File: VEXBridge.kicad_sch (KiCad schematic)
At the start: 87 parts, among them J1 VEX V5, J10 Port 1, J11 Port 2, J12 Port 3, J13 Port 4, J14 USB_C_Receptacle_USB2.0_14P, J2 Port A, J3 Port B, J4 Port C, J5 Port D, J6 Port E, J7 Port F, J8 Port G, J9 Port H, Q1 BSS138, Q2 BSS138, Q3 BSS138, Q4 BSS138, Q5 BSS138, Q6 BSS138, Q7 BSS138, Q8 BSS138, SW1 Reset, SW2 Boot, U1 LMR33630ADDA, U2 AMS1117-3.3, U3 D3V3XA4B10LP, U4 PCA9548ADB, U6 ESP32-S3-MINI-1U, U7 MAX485E

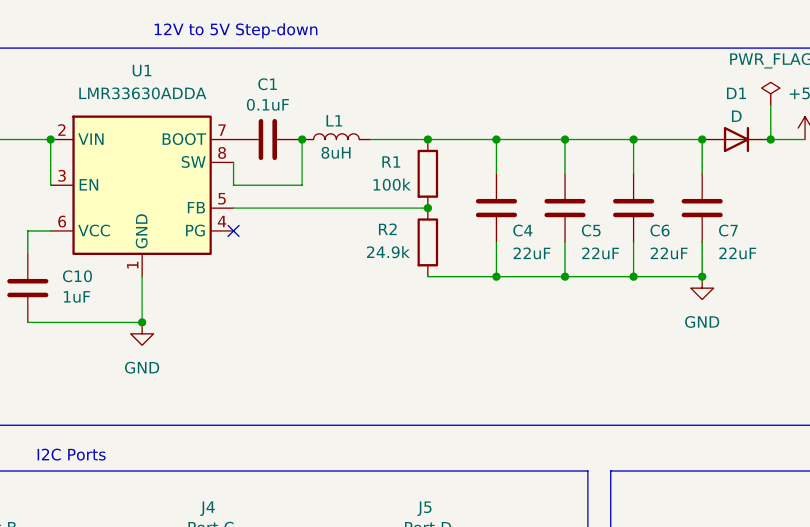
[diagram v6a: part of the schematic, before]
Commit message: Initial PCB Design w/o power rails
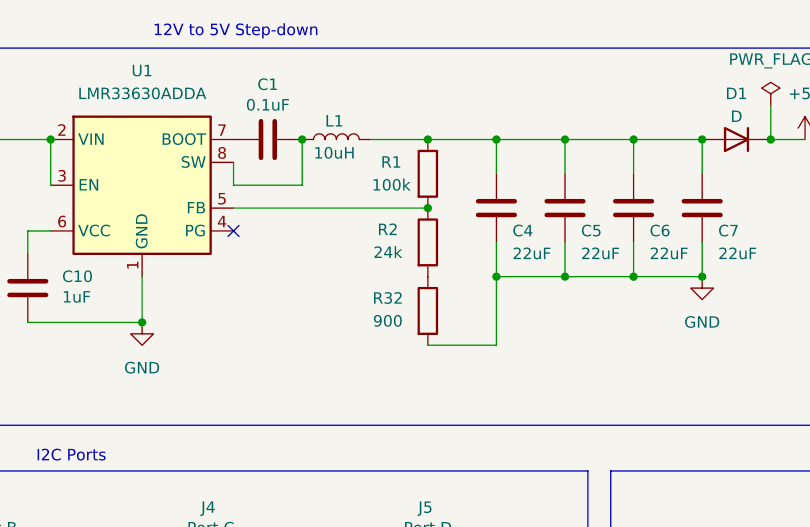
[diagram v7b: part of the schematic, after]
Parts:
- added R32: 900, Resistor_SMD:R_0805_2012Metric, symbol Device:R
- C1, C10, C2: footprint Capacitor_SMD:C_1210_3225Metric -> Capacitor_SMD:C_0603_1608Metric
- C11, C12, C13, C14, C15, C8: footprint Capacitor_SMD:C_0201_0603Metric -> Capacitor_SMD:C_0603_1608Metric
- C3: footprint Capacitor_SMD:C_1210_3225Metric -> Capacitor_SMD:C_0402_1005Metric
- C4, C5, C6, C7, C9: footprint Capacitor_SMD:C_1206_3216Metric -> Capacitor_SMD:C_0603_1608Metric
- D3, D4: footprint (none) -> LED_SMD:LED_0603_1608Metric
- JP2: footprint (none) -> Jumper:SolderJumper-3_P1.3mm_Bridged12_RoundedPad1.0x1.5mm
- L1: value 8uH -> 10uH
- Q1, Q2, Q3, Q4, Q5, Q6, Q7, Q8: footprint Package_TO_SOT_SMD:SOT-23 -> Package_TO_SOT_SMD:SOT-23-3
- R2: value 24.9k -> 24k
- SW1, SW2: footprint (none) -> Button_Switch_SMD:SW_SPST_TS-1088-xR020
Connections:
- net GND: now also R32.2; no longer R2.2
- new net: R2.2, R32.1
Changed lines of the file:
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@@
 	)
 	(junction
-		(at 182.88 43.18)
-		(diameter 0)
-		(color 0 0 0 0)
-	)
-	(junction
 		(at 24.13 167.64)
 		(diameter 0)
@@
 	)
 	(junction
+		(at 182.88 43.18)
+		(diameter 0)
+		(color 0 0 0 0)
+	)
+	(junction
 		(at 93.98 199.39)
 		(diameter 0)
@@
 	(wire
 		(pts
+			(xy 175.26 50.8) (xy 182.88 50.8)
+		)
+		(stroke
+			(width 0)
+			(type default)
+		)
+	)
+	(wire
+		(pts
 			(xy 182.88 170.18) (xy 184.15 170.18)
 		)
@@
 	(wire
 		(pts
-			(xy 175.26 43.18) (xy 182.88 43.18)
-		)
-		(stroke
-			(width 0)
-			(type default)
-		)
-	)
-	(wire
-		(pts
 			(xy 240.03 95.25) (xy 242.57 95.25)
 		)
@@
 	(wire
 		(pts
+			(xy 182.88 50.8) (xy 182.88 43.18)
+		)
+		(stroke
+			(width 0)
+			(type default)
+		)
+	)
+	(wire
+		(pts
 			(xy 96.52 39.37) (xy 96.52 43.18)
 		)
@@
 	)
 	(symbol
+		(lib_id "Device:R")
+		(at 175.26 46.99 0)
+		(unit 1)
+		(exclude_from_sim no)
+		(in_bom yes)
+		(on_board yes)
+		(dnp no)
+		(property "Reference" "R32"
+			(at 170.815 45.593 0)
+			(effects
+				(font
+					(size 1.27 1.27)
+				)
+			)
+		)
+		(property "Value" "900"
+			(at 170.815 48.133 0)
+			(effects
+				(font
+					(size 1.27 1.27)
+				)
+			)
+		)
+		(property "Footprint" "Resistor_SMD:R_0805_2012Metric"
+			(at 173.482 46.99 90)
+			(effects
+				(font
+					(size 1.27 1.27)
+				)
+				(hide yes)
+			)
+		)
+		(property "Datasheet" "~"
+			(at 175.26 46.99 0)
+			(effects
+				(font
+					(size 1.27 1.27)
+				)
+				(hide yes)
+			)
+		)
+		(property "Description" "Resistor"
+			(at 175.26 46.99 0)
+			(effects
+				(font
+					(size 1.27 1.27)
+				)
+				(hide yes)
+			)
+		)
+		(pin "1"
+		)
+		(pin "2"
+		)
+		(instances
+			(project "VEXBridge"
+				(path "/75715a9c-a502-40d6-b270-e5c0bc6847fe"
+					(reference "R32")
+					(unit 1)
+				)
+			)
+		)
+	)
+	(symbol
 		(lib_id "power:+5V")
 		(at 130.81 135.89 0)
@@
 			)
 		)
-		(property "Footprint" "Capacitor_SMD:C_0201_0603Metric"
+		(property "Footprint" "Capacitor_SMD:C_0603_1608Metric"
 			(at 234.6452 41.91 0)
 			(effects
@@
 			)
 		)
-		(property "Footprint" "Capacitor_SMD:C_0201_0603Metric"
+		(property "Footprint" "Capacitor_SMD:C_0603_1608Metric"
 			(at 86.0552 207.01 0)
 			(effects
@@
 			)
 		)
-		(property "Footprint" "Capacitor_SMD:C_1210_3225Metric"
+		(property "Footprint" "Capacitor_SMD:C_0603_1608Metric"
 			(at 97.4852 39.37 0)
 			(effects
@@
 			)
 		)
-		(property "Footprint" "Capacitor_SMD:C_1206_3216Metric"
+		(property "Footprint" "Capacitor_SMD:C_0603_1608Metric"
 			(at 183.8452 39.37 0)
 			(effects
@@
 			)
 		)
-		(property "Footprint" ""
+		(property "Footprint" "Button_Switch_SMD:SW_SPST_TS-1088-xR020"
 			(at 313.69 185.42 0)
 			(effects
@@
 			)
 		)
-		(property "Footprint" "Capacitor_SMD:C_1210_3225Metric"
+		(property "Footprint" "Capacitor_SMD:C_0402_1005Metric"
 			(at 110.1852 39.37 0)
 			(effects
@@
 			)
 		)
-		(property "Footprint" ""
+		(property "Footprint" "LED_SMD:LED_0603_1608Metric"
 			(at 256.54 184.15 0)
 			(effects
@@
 			)
 		)
-		(property "Footprint" "Package_TO_SOT_SMD:SOT-23"
+		(property "Footprint" "Package_TO_SOT_SMD:SOT-23-3"
 			(at 175.895 172.72 0)
 			(effects
@@
 			)
 		)
-		(property "Footprint" "Package_TO_SOT_SMD:SOT-23"
+		(property "Footprint" "Package_TO_SOT_SMD:SOT-23-3"
 			(at 95.885 146.05 0)
 			(effects
@@
 			)
 		)
-		(property "Footprint" "Capacitor_SMD:C_1206_3216Metric"
+		(property "Footprint" "Capacitor_SMD:C_0603_1608Metric"
 			(at 268.9352 41.91 0)
 			(effects
@@
 			)
 		)
-		(property "Footprint" "Package_TO_SOT_SMD:SOT-23"
+		(property "Footprint" "Package_TO_SOT_SMD:SOT-23-3"
 			(at 149.225 172.72 0)
 			(effects
@@
 			)
 		)
-		(property "Footprint" "Package_TO_SOT_SMD:SOT-23"
+		(property "Footprint" "Package_TO_SOT_SMD:SOT-23-3"
 			(at 175.895 146.05 0)
 			(effects
@@
 			)
 		)
-		(property "Footprint" "Capacitor_SMD:C_1206_3216Metric"
+		(property "Footprint" "Capacitor_SMD:C_0603_1608Metric"
 			(at 191.4652 39.37 0)
 			(effects
@@
 			)
 		)
-		(property "Value" "24.9k"
+		(property "Value" "24k"
 			(at 170.815 40.513 0)
 			(effects
@@
 			)
 		)
-		(property "Footprint" "Capacitor_SMD:C_1206_3216Metric"
+		(property "Footprint" "Capacitor_SMD:C_0603_1608Metric"
 			(at 199.0852 39.37 0)
 			(effects
@@
 			)
 		)
-		(property "Footprint" ""
+		(property "Footprint" "Button_Switch_SMD:SW_SPST_TS-1088-xR020"
 			(at 341.63 185.42 0)
 			(effects
@@
 			)
 		)
-		(property "Footprint" "Capacitor_SMD:C_1206_3216Metric"
+		(property "Footprint" "Capacitor_SMD:C_0603_1608Metric"
 			(at 206.7052 39.37 0)
 			(effects
@@
 			)
 		)
-		(property "Value" "8uH"
-			(at 163.322 29.464 90)
+		(property "Value" "10uH"
+			(at 162.56 29.464 90)
 			(effects
 				(font
@@
 			)
 		)
-		(property "Footprint" "Package_TO_SOT_SMD:SOT-23"
+		(property "Footprint" "Package_TO_SOT_SMD:SOT-23-3"
 			(at 95.885 172.72 0)
 			(effects
@@
 			)
 		)
-		(property "Footprint" "Capacitor_SMD:C_1210_3225Metric"
+		(property "Footprint" "Capacitor_SMD:C_0603_1608Metric"
 			(at 131.7752 48.26 0)
 			(effects
@@
 			)
 		)
-		(property "Footprint" ""
+		(property "Footprint" "LED_SMD:LED_0603_1608Metric"
 			(at 223.52 182.88 0)
 			(effects
@@
 			)
 		)
-		(property "Footprint" "Capacitor_SMD:C_0201_0603Metric"
+		(property "Footprint" "Capacitor_SMD:C_0603_1608Metric"
 			(at 336.2452 83.82 0)
 			(effects
@@
 			)
 		)
-		(property "Footprint" "Capacitor_SMD:C_0201_0603Metric"
+		(property "Footprint" "Capacitor_SMD:C_0603_1608Metric"
 			(at 45.4152 78.74 0)
 			(effects
@@
 			)
 		)
-		(property "Footprint" "Package_TO_SOT_SMD:SOT-23"
+		(property "Footprint" "Package_TO_SOT_SMD:SOT-23-3"
 			(at 122.555 146.05 0)
 			(effects
@@
 			)
 		)
-		(property "Footprint" "Capacitor_SMD:C_0201_0603Metric"
+		(property "Footprint" "Capacitor_SMD:C_0603_1608Metric"
 			(at 301.9552 189.23 0)
 			(effects
@@
 			)
 		)
-		(property "Footprint" "Capacitor_SMD:C_0201_0603Metric"
+		(property "Footprint" "Capacitor_SMD:C_0603_1608Metric"
 			(at 348.9452 83.82 0)
 			(effects
@@
 			)
 		)
-		(property "Footprint" "Capacitor_SMD:C_1210_3225Metric"
+		(property "Footprint" "Capacitor_SMD:C_0603_1608Metric"
 			(at 161.29 26.9748 0)
 			(effects
@@
 			)
 		)
-		(property "Footprint" "Package_TO_SOT_SMD:SOT-23"
+		(property "Footprint" "Package_TO_SOT_SMD:SOT-23-3"
 			(at 122.555 172.72 0)
 			(effects
@@
 			)
 		)
-		(property "Footprint" ""
+		(property "Footprint" "Jumper:SolderJumper-3_P1.3mm_Bridged12_RoundedPad1.0x1.5mm"
 			(at 236.22 146.05 0)
 			(effects
@@
 			)
 		)
-		(property "Footprint" "Package_TO_SOT_SMD:SOT-23"
+		(property "Footprint" "Package_TO_SOT_SMD:SOT-23-3"
 			(at 149.225 146.05 0)
 			(effects

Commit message: Near-Final PCB Design
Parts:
- removed D1, D2: D, Diode_SMD:D_0201_0603Metric, symbol Device:D
- removed J14: USB_C_Receptacle_USB2.0_14P, Connector_USB:USB_C_Plug_Molex_105444, symbol Connector:USB_C_Receptacle_USB2.0_14P
- removed U4: PCA9548ADB, Package_SO:SSOP-24_5.3x8.2mm_P0.65mm, symbol Interface_Expansion:PCA9548ADB
- added J15: USB_C_Receptacle, Connector_USB:USB_C_Receptacle_Molex_105450-0101, symbol Connector:USB_C_Receptacle
- added U5: TCA9548APWR, Package_SO:TSSOP-24_4.4x7.8mm_P0.65mm, symbol Interface_Expansion:TCA9548APWR
- C14, C4, C5, C6, C7, C9: footprint Capacitor_SMD:C_0603_1608Metric -> Capacitor_SMD:C_0805_2012Metric
- D4: value BLUE -> GREEN
- F1: footprint Fuse:Fuse_2010_5025Metric -> Fuse:Fuse_1812_4532Metric
- L1: footprint Inductor_SMD:L_0603_1608Metric -> Inductor_SMD:L_TechFuse_SL0420
- R26: value 4.7k -> 330
- R27: value 2.2k -> 150
- R32: value 900 -> 820; footprint Resistor_SMD:R_0805_2012Metric -> Resistor_SMD:R_0603_1608Metric
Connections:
- net +3.3V: now also U5.24 (VCC)
- net +5V: now also C4.1, C5.1, C6.1, C7.1, L1.2, R1.1
- net A: no longer U3.1
- net B: no longer U3.2
- net GND: now also J15.A1 (GND), J15.A12 (GND), J15.B1 (GND), J15.B12 (GND), J15.S1 (SHIELD), U5.1 (A0), U5.12 (GND), U5.2 (A1)
- net Multi_ADDR: now also U5.21 (A2)
- net SCL: now also U5.22 (SCL)
- net SCL1: now also U5.5 (SC0)
- net SCL2: now also U5.7 (SC1)
- net SCL3: now also U5.9 (SC2)
- net SCL4: now also U5.11 (SC3)
- net SCL5: now also U5.14 (SC4)
- net SCL6: now also U5.16 (SC5)
- net SCL7: now also U5.18 (SC6)
- net SCL8: now also U5.20 (SC7)
- net SDA: now also U5.23 (SDA)
- net SDA1: now also U5.4 (SD0)
- net SDA2: now also U5.6 (SD1)
- net SDA3: now also U5.8 (SD2)
- net SDA4: now also U5.10 (SD3)
- net SDA5: now also U5.13 (SD4)
- net SDA6: now also U5.15 (SD5)
- net SDA7: now also U5.17 (SD6)
- net SDA8: now also U5.19 (SD7)
- net USB_D+: now also J15.A6 (D+), J15.B6 (D+)
- net USB_D-: now also J15.A7 (D-), J15.B7 (D-)
- net at R24.1: now also J15.B5 (CC2)
- net at R25.1: now also J15.A5 (CC1)
- net at R6.2: now also U5.3 (~{RESET})
- new net: J15.A4 (VBUS), J15.A9 (VBUS), J15.B4 (VBUS), J15.B9 (VBUS)
- no-connect marks 25 -> 38
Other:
- moved on the sheet: D3, D4, JP2, R24, R25, R26, R27
